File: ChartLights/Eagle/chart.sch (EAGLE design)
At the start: 8 parts, among them J0 0, J1 0, U0 TLC5916IN, U1 TLC5916IN

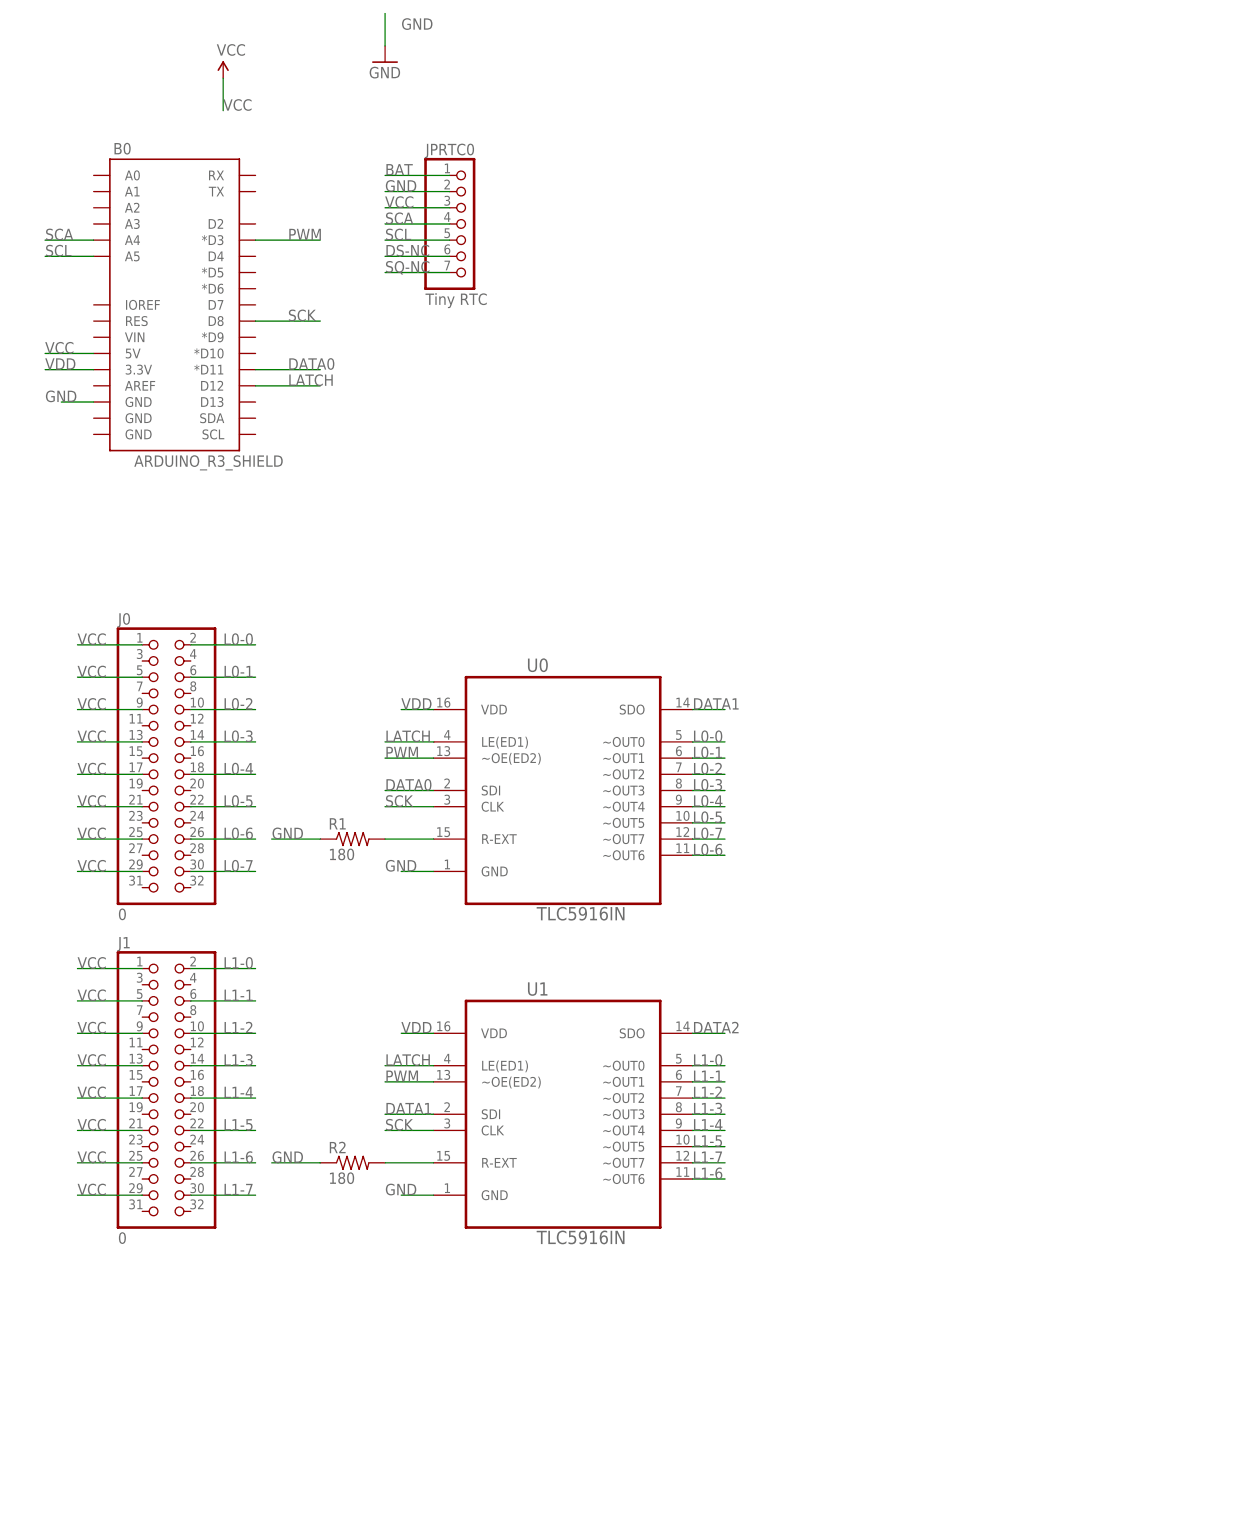
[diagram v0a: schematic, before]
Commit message: 2x20 headers x2, all on one UnoR3 header
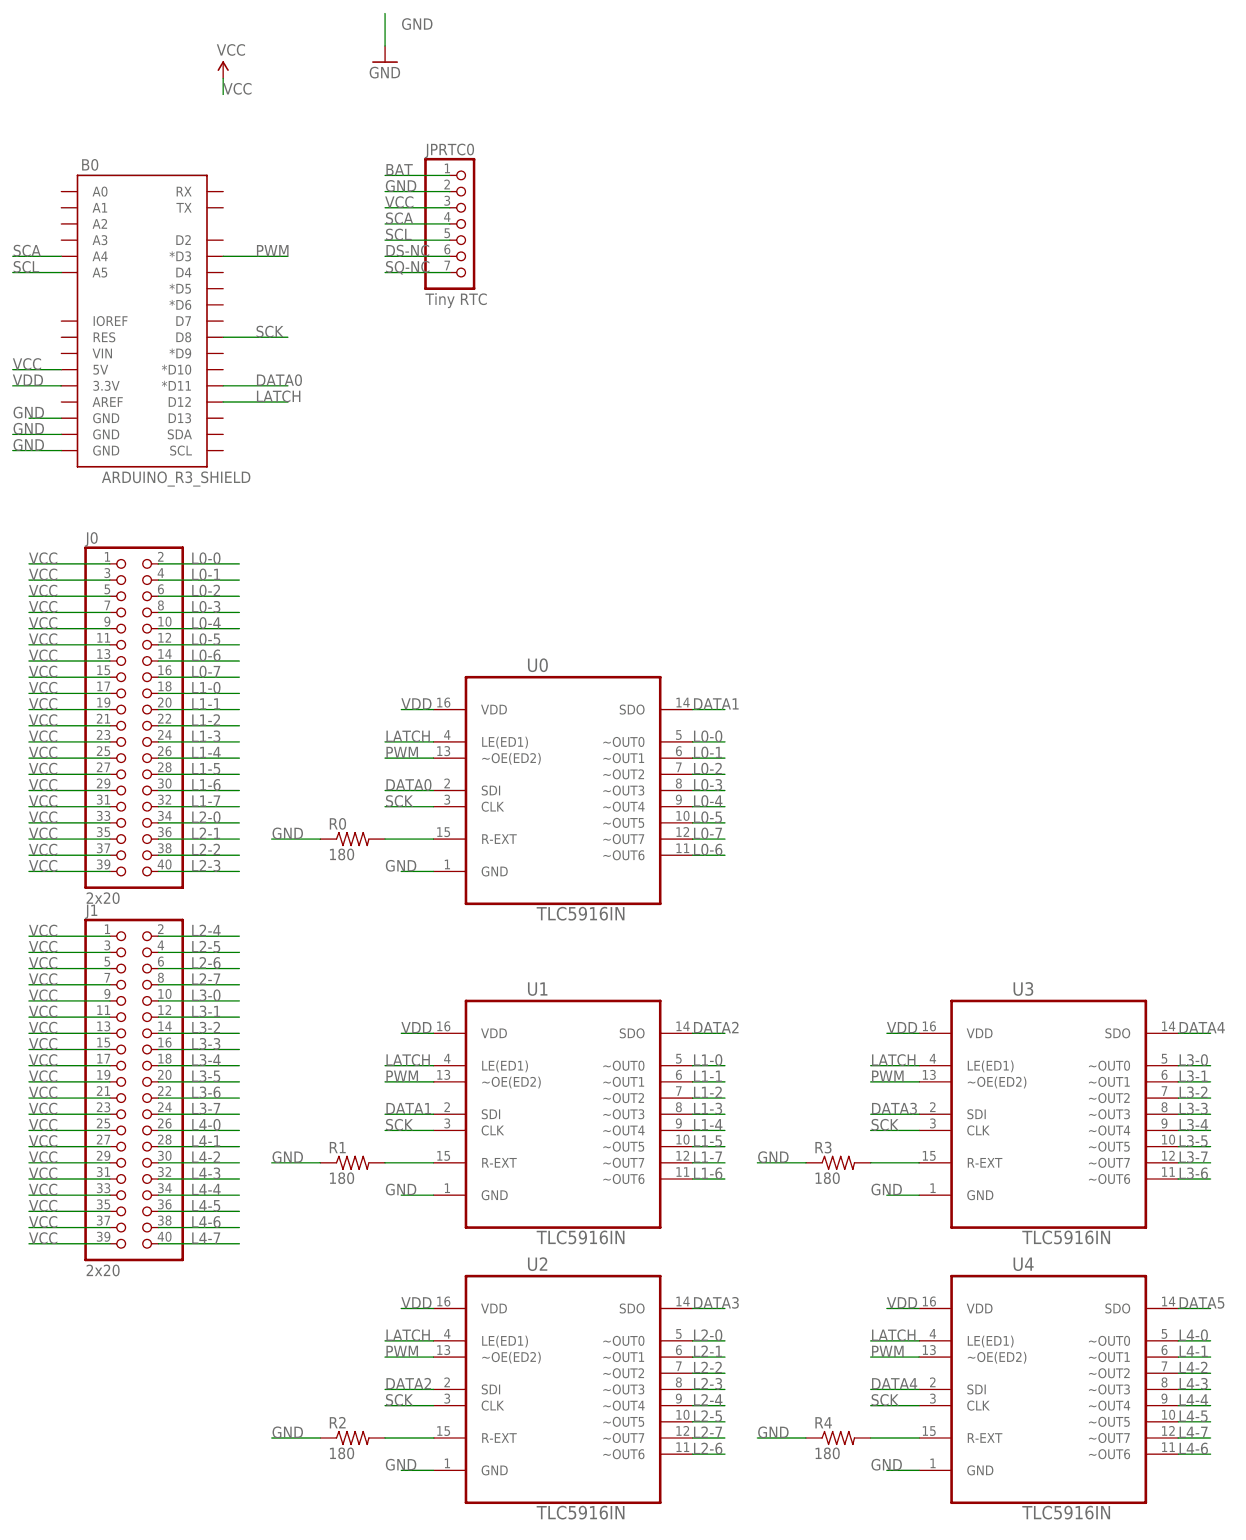
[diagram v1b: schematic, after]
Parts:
- added R0, R3, R4: 180, SparkFun-Resistors:RESISTORPTH-1/4W
- added U2, U3, U4: TLC5916IN, Texas Instruments_By_element14_Batch_1:TLC5916IN
- J0, J1: value 0 -> 2x20; device pinhead:PINHD-2X16 -> pinhead:PINHD-2X20/90
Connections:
- new net DATA3: U2.SDO, U3.SDI
- new net DATA4: U3.SDO, U4.SDI
- new net DATA5: U4.SDO
- new net L2-0: J0.34, U2.~OUT0
- new net L2-1: J0.36, U2.~OUT1
- new net L2-2: J0.38, U2.~OUT2
- new net L2-3: J0.40, U2.~OUT3
- new net L2-4: J1.2, U2.~OUT4
- new net L2-5: J1.4, U2.~OUT5
- new net L2-6: J1.6, U2.~OUT6
- new net L2-7: J1.8, U2.~OUT7
- new net L3-0: J1.10, U3.~OUT0
- new net L3-1: J1.12, U3.~OUT1
- new net L3-2: J1.14, U3.~OUT2
- new net L3-3: J1.16, U3.~OUT3
- new net L3-4: J1.18, U3.~OUT4
- new net L3-5: J1.20, U3.~OUT5
- new net L3-6: J1.22, U3.~OUT6
- new net L3-7: J1.24, U3.~OUT7
- new net L4-0: J1.26, U4.~OUT0
- new net L4-1: J1.28, U4.~OUT1
- new net L4-2: J1.30, U4.~OUT2
- new net L4-3: J1.32, U4.~OUT3
- new net L4-4: J1.34, U4.~OUT4
- new net L4-5: J1.36, U4.~OUT5
- new net L4-6: J1.38, U4.~OUT6
- new net L4-7: J1.40, U4.~OUT7
- new net N$2: R2.2, U2.R-EXT
- new net N$3: R3.2, U3.R-EXT
- new net N$4: R4.2, U4.R-EXT
- net DATA2: now also U2.SDI
- net GND: now also B0.GND@0, B0.GND@1, R0.1, R3.1, R4.1, U2.GND, U3.GND, U4.GND
- net L0-1: now also J0.4; no longer J0.6
- net L0-2: now also J0.6; no longer J0.10
- net L0-3: now also J0.8; no longer J0.14
- net L0-4: now also J0.10; no longer J0.18
- net L0-5: now also J0.12; no longer J0.22
- net L0-6: now also J0.14; no longer J0.26
- net L0-7: now also J0.16; no longer J0.30
- net L1-0: now also J0.18; no longer J1.2
- net L1-1: now also J0.20; no longer J1.6
- net L1-2: now also J0.22; no longer J1.10
- net L1-3: now also J0.24; no longer J1.14
- net L1-4: now also J0.26; no longer J1.18
- net L1-5: now also J0.28; no longer J1.22
- net L1-6: now also J0.30; no longer J1.26
- net L1-7: now also J0.32; no longer J1.30
- net LATCH: now also U2.LE(ED1), U3.LE(ED1), U4.LE(ED1)
- net N$1: now also R1.2; no longer R2.2
- net N$6: now also R0.2; no longer R1.2
- net PWM: now also U2.~OE(ED2), U3.~OE(ED2), U4.~OE(ED2)
- net SCK: now also U2.CLK, U3.CLK, U4.CLK
- net VCC: now also J0.11, J0.15, J0.19, J0.23, J0.27, J0.3, J0.31, J0.33, J0.35, J0.37, J0.39, J0.7, J1.11, J1.15, J1.19, J1.23, J1.27, J1.3, J1.31, J1.33, J1.35, J1.37, J1.39, J1.7
- net VDD: now also U2.VDD, U3.VDD, U4.VDD
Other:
- moved on the sheet: B0, R1, R2
